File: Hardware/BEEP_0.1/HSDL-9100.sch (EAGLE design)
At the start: 6 parts, among them IC1 HSDL-9100

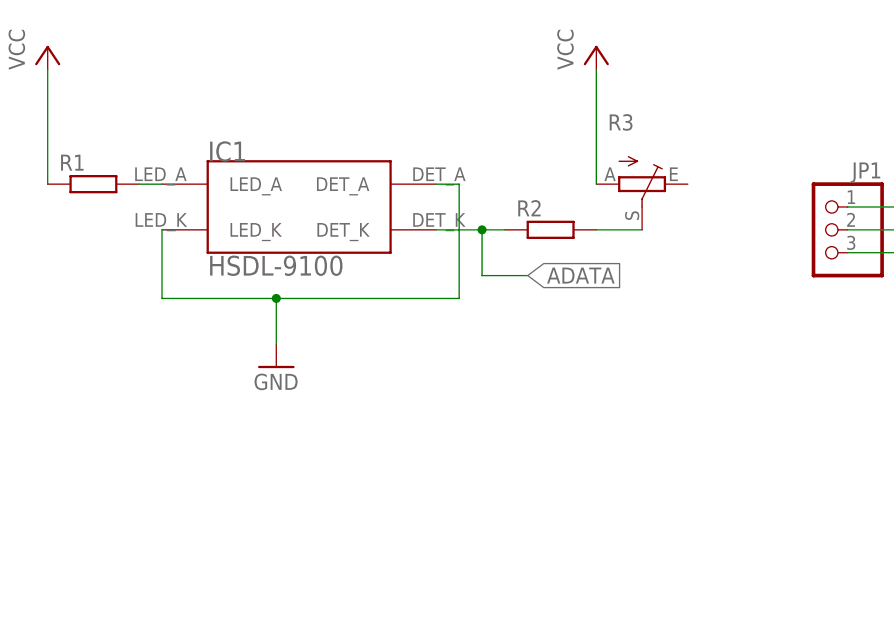
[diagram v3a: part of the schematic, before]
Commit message: enhance pads and board for HSDL-9100
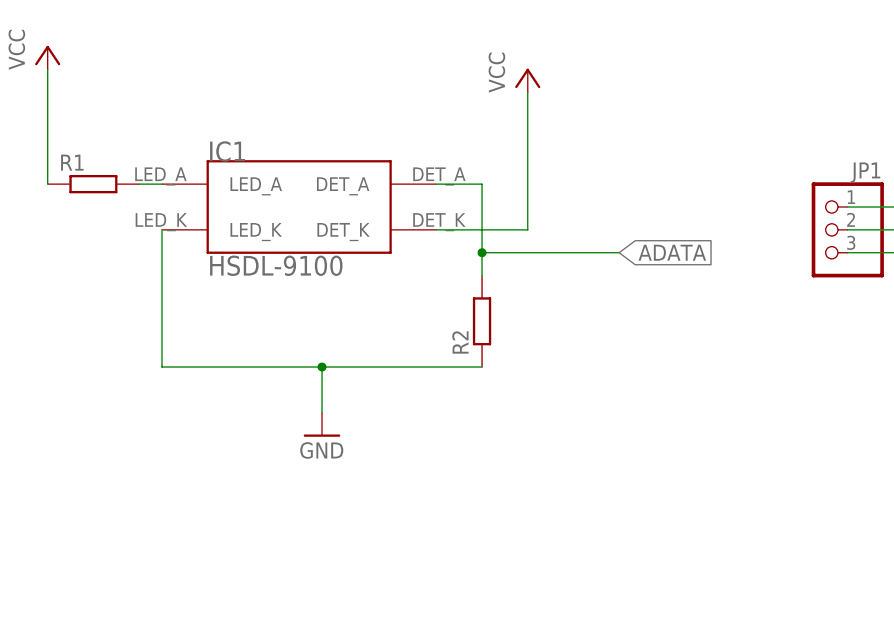
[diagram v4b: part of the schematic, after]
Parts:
- removed R3: (no value), pot:TRIM_EU-B25P
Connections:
- removed net N$5: R2.2, R3.S
- net ADATA: now also IC1.DET_A, R2.2; no longer IC1.DET_K, R2.1
- net GND: now also R2.1; no longer IC1.DET_A
- net VCC: now also IC1.DET_K; no longer R3.A
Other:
- moved on the sheet: R2
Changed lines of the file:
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@@
 <part name="U$1" library="Branding" deviceset="LOGO-COPPER" device="3" value="LOGO-COPPER3"/>
 <part name="R2" library="rcl" deviceset="R-EU_" device="M0805"/>
-<part name="R3" library="pot" deviceset="TRIM_EU-" device="B25P"/>
 <part name="P+1" library="supply1" deviceset="VCC" device=""/>
 <part name="P+2" library="supply1" deviceset="VCC" device=""/>
@@
 <instance part="FRAME1" gate="G$1" x="0" y="0"/>
 <instance part="U$1" gate="G$1" x="185.42" y="12.7"/>
-<instance part="R2" gate="G$1" x="157.48" y="93.98"/>
-<instance part="R3" gate="1" x="167.64" y="99.06" rot="R270"/>
-<instance part="P+1" gate="VCC" x="162.56" y="114.3"/>
+<instance part="R2" gate="G$1" x="149.86" y="83.82" rot="R90"/>
+<instance part="P+1" gate="VCC" x="154.94" y="111.76"/>
 <instance part="P+2" gate="VCC" x="101.6" y="114.3"/>
-<instance part="GND1" gate="1" x="127" y="78.74"/>
+<instance part="GND1" gate="1" x="132.08" y="71.12"/>
 <instance part="P+3" gate="VCC" x="213.36" y="104.14"/>
 <instance part="GND2" gate="1" x="213.36" y="86.36"/>
@@
 <segment>
 <pinref part="IC1" gate="G$1" pin="LED_K"/>
-<wire x1="114.3" y1="93.98" x2="114.3" y2="86.36" width="0.1524" layer="91"/>
-<wire x1="114.3" y1="86.36" x2="127" y2="86.36" width="0.1524" layer="91"/>
+<wire x1="114.3" y1="93.98" x2="114.3" y2="78.74" width="0.1524" layer="91"/>
+<wire x1="114.3" y1="78.74" x2="132.08" y2="78.74" width="0.1524" layer="91"/>
 <pinref part="GND1" gate="1" pin="GND"/>
-<pinref part="IC1" gate="G$1" pin="DET_A"/>
-<wire x1="127" y1="86.36" x2="127" y2="81.28" width="0.1524" layer="91"/>
-<wire x1="144.78" y1="99.06" x2="147.32" y2="99.06" width="0.1524" layer="91"/>
-<wire x1="147.32" y1="86.36" x2="147.32" y2="99.06" width="0.1524" layer="91"/>
-<wire x1="147.32" y1="86.36" x2="127" y2="86.36" width="0.1524" layer="91"/>
-<junction x="127" y="86.36"/>
+<wire x1="132.08" y1="78.74" x2="132.08" y2="73.66" width="0.1524" layer="91"/>
+<wire x1="149.86" y1="78.74" x2="132.08" y2="78.74" width="0.1524" layer="91"/>
+<junction x="132.08" y="78.74"/>
+<pinref part="R2" gate="G$1" pin="1"/>
 </segment>
 <segment>
 <pinref part="GND2" gate="1" pin="GND"/>
+<pinref part="JP1" gate="A" pin="2"/>
 <wire x1="190.5" y1="93.98" x2="213.36" y2="93.98" width="0.1524" layer="91"/>
 <wire x1="213.36" y1="93.98" x2="213.36" y2="88.9" width="0.1524" layer="91"/>
-<pinref part="JP1" gate="A" pin="2"/>
 </segment>
 </net>
@@
 <net name="ADATA" class="0">
 <segment>
-<pinref part="IC1" gate="G$1" pin="DET_K"/>
-<pinref part="R2" gate="G$1" pin="1"/>
-<wire x1="144.78" y1="93.98" x2="149.86" y2="93.98" width="0.1524" layer="91"/>
-<wire x1="149.86" y1="93.98" x2="152.4" y2="93.98" width="0.1524" layer="91"/>
-<wire x1="149.86" y1="93.98" x2="149.86" y2="88.9" width="0.1524" layer="91"/>
-<junction x="149.86" y="93.98"/>
-<wire x1="149.86" y1="88.9" x2="154.94" y2="88.9" width="0.1524" layer="91"/>
-<label x="154.94" y="88.9" size="1.778" layer="95" xref="yes"/>
+<wire x1="149.86" y1="91.44" x2="165.1" y2="91.44" width="0.1524" layer="91"/>
+<label x="165.1" y="91.44" size="1.778" layer="95" xref="yes"/>
+<pinref part="IC1" gate="G$1" pin="DET_A"/>
+<pinref part="R2" gate="G$1" pin="2"/>
+<wire x1="144.78" y1="99.06" x2="149.86" y2="99.06" width="0.1524" layer="91"/>
+<wire x1="149.86" y1="99.06" x2="149.86" y2="91.44" width="0.1524" layer="91"/>
+<wire x1="149.86" y1="91.44" x2="149.86" y2="88.9" width="0.1524" layer="91"/>
+<junction x="149.86" y="91.44"/>
 </segment>
 <segment>
@@
 </segment>
 </net>
-<net name="N$5" class="0">
-<segment>
-<pinref part="R2" gate="G$1" pin="2"/>
-<pinref part="R3" gate="1" pin="S"/>
-<wire x1="162.56" y1="93.98" x2="167.64" y2="93.98" width="0.1524" layer="91"/>
-</segment>
-</net>
 <net name="VCC" class="0">
 <segment>
-<pinref part="R3" gate="1" pin="A"/>
-<wire x1="162.56" y1="99.06" x2="162.56" y2="111.76" width="0.1524" layer="91"/>
+<wire x1="154.94" y1="93.98" x2="154.94" y2="109.22" width="0.1524" layer="91"/>
 <pinref part="P+1" gate="VCC" pin="VCC"/>
+<pinref part="IC1" gate="G$1" pin="DET_K"/>
+<wire x1="144.78" y1="93.98" x2="154.94" y2="93.98" width="0.1524" layer="91"/>
 </segment>
 <segment>
